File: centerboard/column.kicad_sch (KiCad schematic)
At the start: 9 parts, among them J1 Conn_01x10_MountingPin

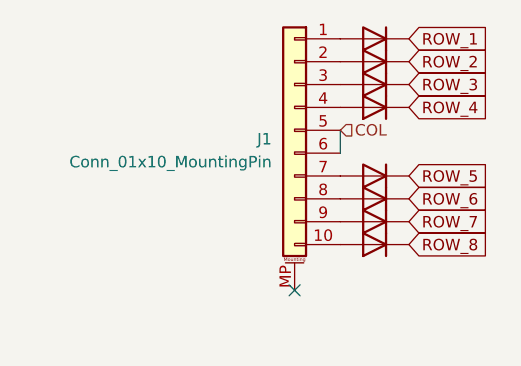
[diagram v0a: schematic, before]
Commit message: Rework centerboard yet again. Now with vertical FFC headers and a ground pour.
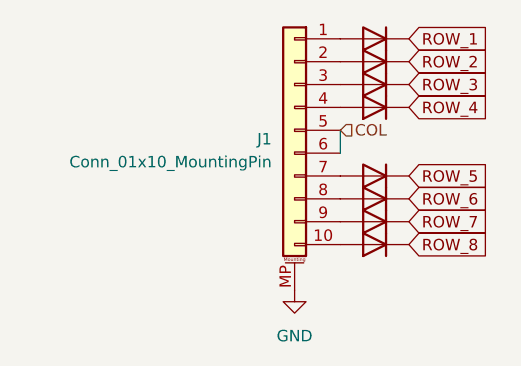
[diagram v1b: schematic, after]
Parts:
- J1: footprint Custom:FFC_Clamshell_0.5mm_1x10 -> Custom:GCT_FFC2A33-10-T-R_REVA
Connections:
- net GND: now reaches J1.MP (MountPin)
- no-connect marks 1 -> 0
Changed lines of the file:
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@@
 (kicad_sch (version 20230121) (generator eeschema)
   (paper "A4")
-  (no_connect (at 154.94 140.97))
   (wire (pts (xy 160.02 123.19) (xy 160.02 125.73))
     (stroke (width 0) (type default))
@@
         (path "/4cf5c873-f5e9-4261-911c-886f387fb0f3/e4834520-9e93-41c6-9dec-c6197700f3e4"
           (reference "D46") (unit 1)
+        )
+      )
+    )
+  )
+  (symbol (lib_id "power:GND") (at 154.94 140.97 0) (unit 1)
+    (in_bom yes) (on_board yes) (dnp no) (fields_autoplaced)
+    (property "Reference" "#PWR011" (at 154.94 147.32 0)
+      (effects (font (size 1.27 1.27)) hide)
+    )
+    (property "Value" "GND" (at 154.94 146.05 0)
+      (effects (font (size 1.27 1.27)))
+    )
+    (property "Footprint" "" (at 154.94 140.97 0)
+      (effects (font (size 1.27 1.27)) hide)
+    )
+    (property "Datasheet" "" (at 154.94 140.97 0)
+      (effects (font (size 1.27 1.27)) hide)
+    )
+    (pin "1")
+    (instances
+      (project "centerboard"
+        (path "/4cf5c873-f5e9-4261-911c-886f387fb0f3/e4834520-9e93-41c6-9dec-c6197700f3e4"
+          (reference "#PWR011") (unit 1)
+        )
+        (path "/4cf5c873-f5e9-4261-911c-886f387fb0f3/d5ae333b-0f58-41ed-b117-81002236c64e"
+          (reference "#PWR06") (unit 1)
+        )
+        (path "/4cf5c873-f5e9-4261-911c-886f387fb0f3/749b935f-fa28-4bb9-a8a4-52d11da1282b"
+          (reference "#PWR07") (unit 1)
+        )
+        (path "/4cf5c873-f5e9-4261-911c-886f387fb0f3/d2697422-b7a2-48ac-8df9-88c74b2a539c"
+          (reference "#PWR08") (unit 1)
+        )
+        (path "/4cf5c873-f5e9-4261-911c-886f387fb0f3/db47ecf8-444e-47be-ba3b-f44106296f93"
+          (reference "#PWR09") (unit 1)
+        )
+        (path "/4cf5c873-f5e9-4261-911c-886f387fb0f3/54cfab24-4a53-4928-8700-928a32a39479"
+          (reference "#PWR010") (unit 1)
         )
       )
@@
       (effects (font (size 1.27 1.27)) (justify left))
     )
-    (property "Footprint" "Custom:FFC_Clamshell_0.5mm_1x10" (at 154.94 123.19 0)
-      (effects (font (size 1.27 1.27)) hide)
-    )
+    (property "Footprint" "Custom:GCT_FFC2A33-10-T-R_REVA" (at 154.94 123.19 0)
+      (effects (font (size 1.27 1.27)) hide)
+    )
